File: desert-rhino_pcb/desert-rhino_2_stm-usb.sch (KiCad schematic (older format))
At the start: 1 part

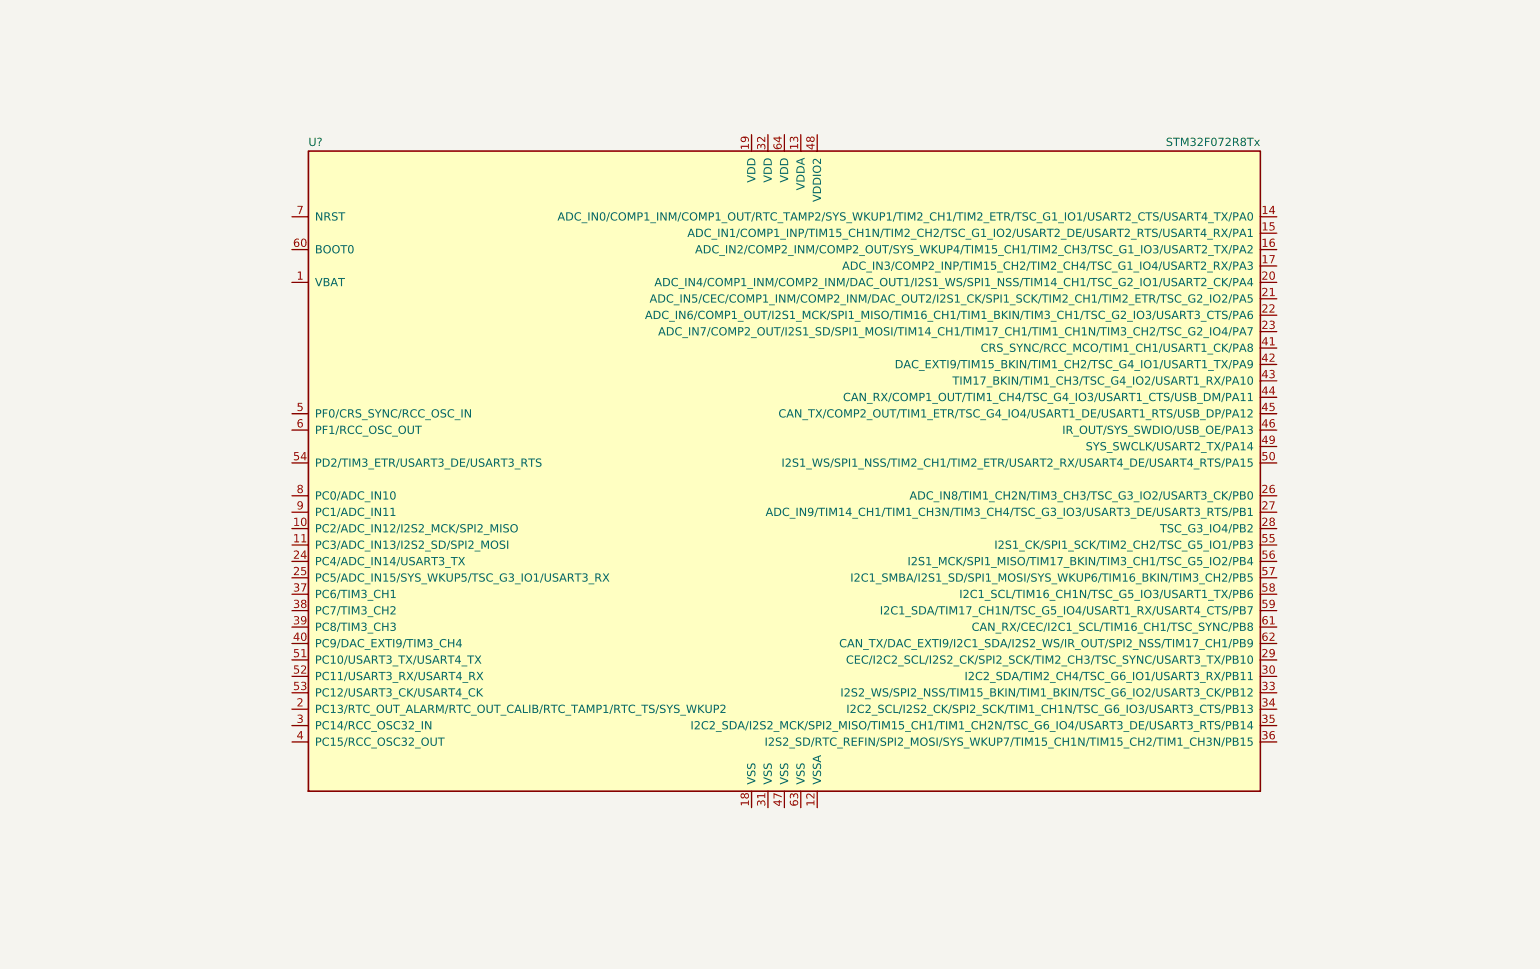
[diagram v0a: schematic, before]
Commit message: Added some bypass caps to STM32
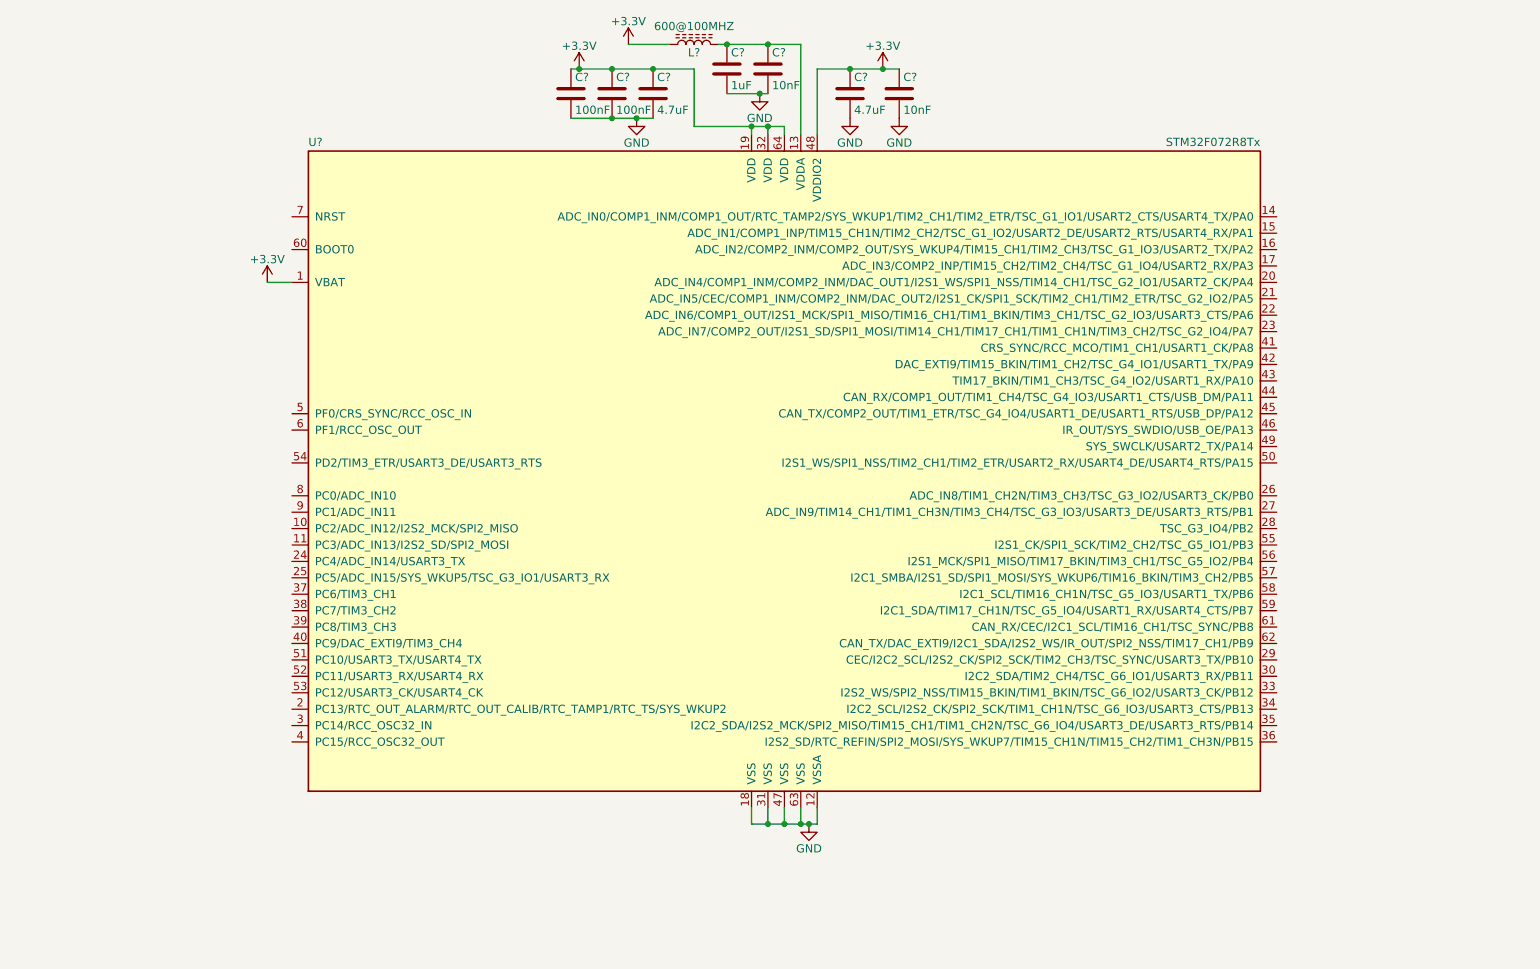
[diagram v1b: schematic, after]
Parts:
- added C?: 1uF, symbol C
- added C? (x2): 10nF, symbol C
- added C? (x2): 4.7uF, symbol C
- added C? (x2): 100nF, symbol C
- added L?: 600@100MHZ, symbol L_Core_Ferrite
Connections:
- net +3V3: now reaches U?.1 (VBAT)
- net +3V3: now also U?.19 (VDD), U?.32 (VDD), U?.48 (VDDIO2), U?.64 (VDD), C?.1, C?.1, C?.1, C?.1, C?.1, L?.1
- net GND: now reaches U?.12 (VSSA)
- net GND: now also U?.18 (VSS), U?.31 (VSS), U?.47 (VSS), U?.63 (VSS), C?.2, C?.2, C?.2, C?.2, C?.2, C?.2, C?.2
- net at U?.13 (VDDA): now also C?.1, C?.1, L?.2

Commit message: Finished most of schem. Still need ina230
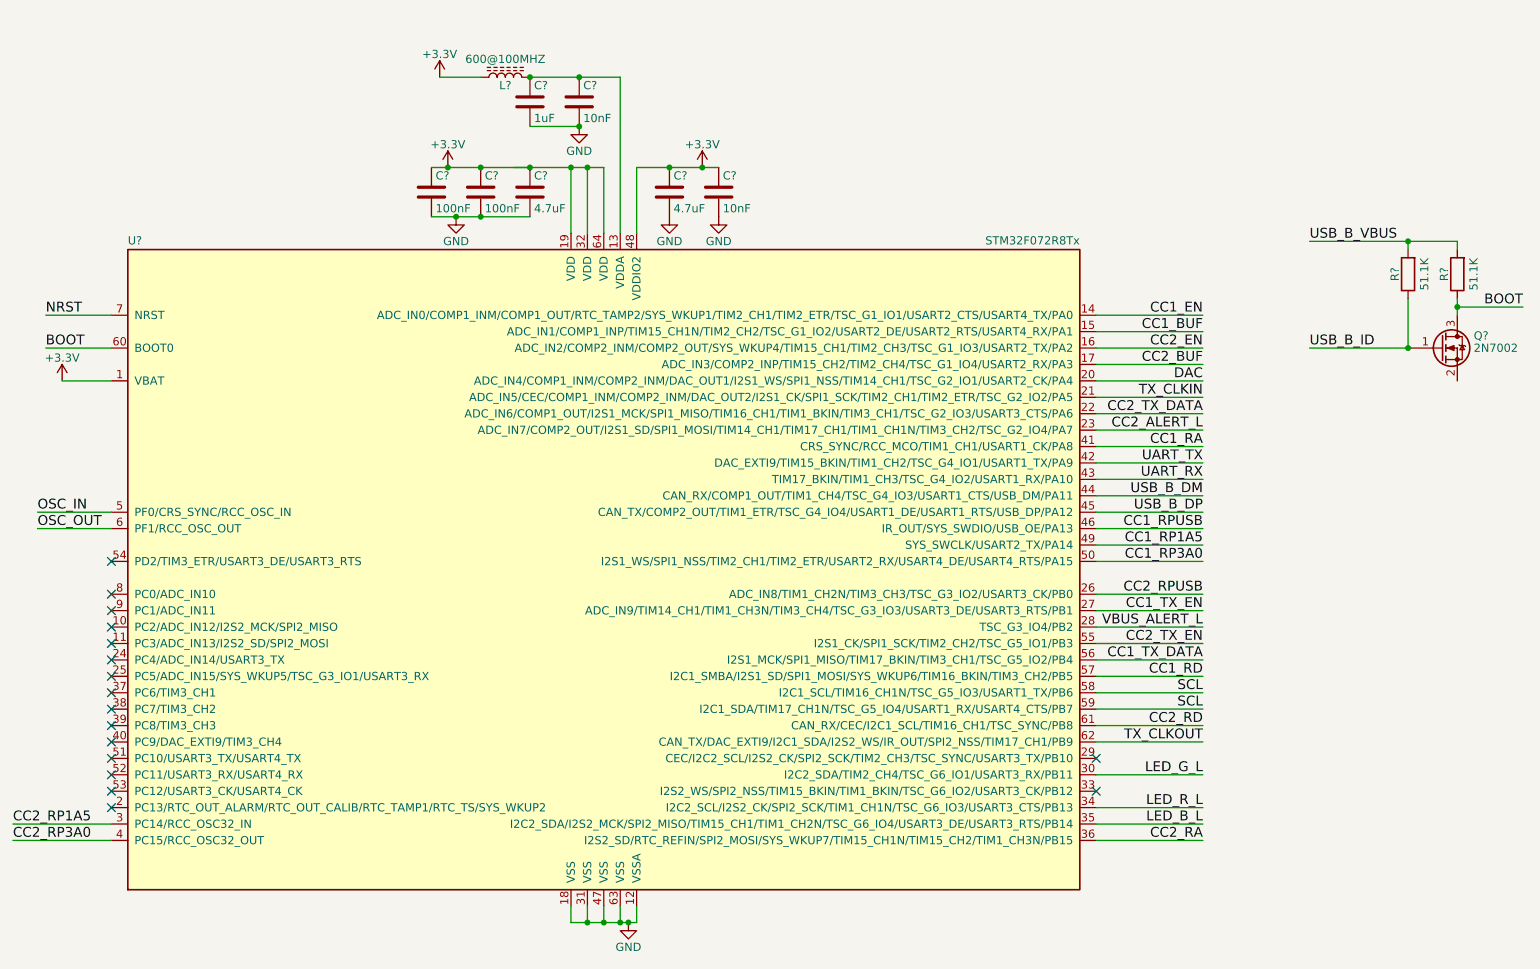
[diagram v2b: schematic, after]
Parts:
- added Q?: 2N7002, TO_SOT_Packages_SMD:SOT-23, symbol 2N7002
- added R? (x2): 51.1K, symbol R
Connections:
- net CC1_EN: now reaches U?.14 (ADC_IN0/COMP1_INM/COMP1_OUT/RTC_TAMP2/SYS_WKUP1/TIM2_CH1/TIM2_ETR/TSC_G1_IO1/USART2_CTS/USART4_TX/PA0)
- net CC1_BUF: now reaches U?.15 (ADC_IN1/COMP1_INP/TIM15_CH1N/TIM2_CH2/TSC_G1_IO2/USART2_DE/USART2_RTS/USART4_RX/PA1)
- net CC2_EN: now reaches U?.16 (ADC_IN2/COMP2_INM/COMP2_OUT/SYS_WKUP4/TIM15_CH1/TIM2_CH3/TSC_G1_IO3/USART2_TX/PA2)
- net CC2_BUF: now reaches U?.17 (ADC_IN3/COMP2_INP/TIM15_CH2/TIM2_CH4/TSC_G1_IO4/USART2_RX/PA3)
- net DAC: now reaches U?.20 (ADC_IN4/COMP1_INM/COMP2_INM/DAC_OUT1/I2S1_WS/SPI1_NSS/TIM14_CH1/TSC_G2_IO1/USART2_CK/PA4)
- net TX_CLKIN: now reaches U?.21 (ADC_IN5/CEC/COMP1_INM/COMP2_INM/DAC_OUT2/I2S1_CK/SPI1_SCK/TIM2_CH1/TIM2_ETR/TSC_G2_IO2/PA5)
- net CC2_TX_DATA: now reaches U?.22 (ADC_IN6/COMP1_OUT/I2S1_MCK/SPI1_MISO/TIM16_CH1/TIM1_BKIN/TIM3_CH1/TSC_G2_IO3/USART3_CTS/PA6)
- net CC2_ALERT_L: now reaches U?.23 (ADC_IN7/COMP2_OUT/I2S1_SD/SPI1_MOSI/TIM14_CH1/TIM17_CH1/TIM1_CH1N/TIM3_CH2/TSC_G2_IO4/PA7)
- net CC2_RPUSB: now reaches U?.26 (ADC_IN8/TIM1_CH2N/TIM3_CH3/TSC_G3_IO2/USART3_CK/PB0)
- net CC1_TX_EN: now reaches U?.27 (ADC_IN9/TIM14_CH1/TIM1_CH3N/TIM3_CH4/TSC_G3_IO3/USART3_DE/USART3_RTS/PB1)
- net VBUS_ALERT_L: now reaches U?.28 (TSC_G3_IO4/PB2)
- net CC2_RP1A5: now reaches U?.3 (PC14/RCC_OSC32_IN)
- net LED_G_L: now reaches U?.30 (I2C2_SDA/TIM2_CH4/TSC_G6_IO1/USART3_RX/PB11)
- net LED_R_L: now reaches U?.34 (I2C2_SCL/I2S2_CK/SPI2_SCK/TIM1_CH1N/TSC_G6_IO3/USART3_CTS/PB13)
- net LED_B_L: now reaches U?.35 (I2C2_SDA/I2S2_MCK/SPI2_MISO/TIM15_CH1/TIM1_CH2N/TSC_G6_IO4/USART3_DE/USART3_RTS/PB14)
- net CC2_RA: now reaches U?.36 (I2S2_SD/RTC_REFIN/SPI2_MOSI/SYS_WKUP7/TIM15_CH1N/TIM15_CH2/TIM1_CH3N/PB15)
- net CC2_RP3A0: now reaches U?.4 (PC15/RCC_OSC32_OUT)
- net CC1_RA: now reaches U?.41 (CRS_SYNC/RCC_MCO/TIM1_CH1/USART1_CK/PA8)
- net UART_TX: now reaches U?.42 (DAC_EXTI9/TIM15_BKIN/TIM1_CH2/TSC_G4_IO1/USART1_TX/PA9)
- net UART_RX: now reaches U?.43 (TIM17_BKIN/TIM1_CH3/TSC_G4_IO2/USART1_RX/PA10)
- net USB_B_DM: now reaches U?.44 (CAN_RX/COMP1_OUT/TIM1_CH4/TSC_G4_IO3/USART1_CTS/USB_DM/PA11)
- net USB_B_DP: now reaches U?.45 (CAN_TX/COMP2_OUT/TIM1_ETR/TSC_G4_IO4/USART1_DE/USART1_RTS/USB_DP/PA12)
- net CC1_RPUSB: now reaches U?.46 (IR_OUT/SYS_SWDIO/USB_OE/PA13)
- net CC1_RP1A5: now reaches U?.49 (SYS_SWCLK/USART2_TX/PA14)
- net OSC_IN: now reaches U?.5 (PF0/CRS_SYNC/RCC_OSC_IN)
- net CC1_RP3A0: now reaches U?.50 (I2S1_WS/SPI1_NSS/TIM2_CH1/TIM2_ETR/USART2_RX/USART4_DE/USART4_RTS/PA15)
- net CC2_TX_EN: now reaches U?.55 (I2S1_CK/SPI1_SCK/TIM2_CH2/TSC_G5_IO1/PB3)
- net CC1_TX_DATA: now reaches U?.56 (I2S1_MCK/SPI1_MISO/TIM17_BKIN/TIM3_CH1/TSC_G5_IO2/PB4)
- net CC1_RD: now reaches U?.57 (I2C1_SMBA/I2S1_SD/SPI1_MOSI/SYS_WKUP6/TIM16_BKIN/TIM3_CH2/PB5)
- net SCL: now reaches U?.58 (I2C1_SCL/TIM16_CH1N/TSC_G5_IO3/USART1_TX/PB6)
- net SCL: now also U?.59 (I2C1_SDA/TIM17_CH1N/TSC_G5_IO4/USART1_RX/USART4_CTS/PB7)
- net OSC_OUT: now reaches U?.6 (PF1/RCC_OSC_OUT)
- net BOOT: now reaches U?.60 (BOOT0)
- net BOOT: now also Q?.3 (D), R?.1
- net CC2_RD: now reaches U?.61 (CAN_RX/CEC/I2C1_SCL/TIM16_CH1/TSC_SYNC/PB8)
- net TX_CLKOUT: now reaches U?.62 (CAN_TX/DAC_EXTI9/I2C1_SDA/I2S2_WS/IR_OUT/SPI2_NSS/TIM17_CH1/PB9)
- net NRST: now reaches U?.7 (NRST)
- new net USB_B_ID: Q?.1 (G), R?.1
- new net USB_B_VBUS: R?.2, R?.2
- no-connect marks 0 -> 17
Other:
- moved on the sheet: C?, L?, U?
